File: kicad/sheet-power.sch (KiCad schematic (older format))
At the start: 18 parts, among them U13 AMS1117-3.3

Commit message: layout and bom complete - waiting on parts from jlcpcb
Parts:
- added D11: b5819w, Diode_SMD:D_SOD-123, symbol Device:D_Schottky_Small
- C31: value 10uf -> 10u; footprint (none) -> Capacitor_SMD:C_0603_1608Metric
- C32, C33, C34, C35, C36, C37, C38, C39, C40: value 100nf -> 100n; footprint (none) -> Capacitor_SMD:C_0402_1005Metric
- C41, C42: value 10uF -> 10u; footprint (none) -> Capacitor_SMD:C_0805_2012Metric
- C43: value 100nF -> 100n; footprint (none) -> Capacitor_SMD:C_0402_1005Metric
- C44: value 10uF -> 10n; footprint (none) -> Capacitor_SMD:C_0402_1005Metric
- D7: footprint (none) -> Diode_SMD:D_SOD-123
- FB1, FB2: footprint (none) -> Inductor_SMD:L_0805_2012Metric
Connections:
- net at D7.1 (K), FB1.2: now also D11.1 (K)
- new net ALT_POWER: D11.2 (A)
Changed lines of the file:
@@
 AR Path="/6020FDCC/60239D67" Ref="FB1"  Part="1"
 F 0 "FB1" V 1863 2950 50  0000 C CNN
-F 1 "100 @ 100Mhz" V 1954 2950 50  0000 C CNN
-F 2 "" V 2030 2950 50  0001 C CNN
+F 1 "100 @ 100Mhz" V 1950 3000 50  0000 C CNN
+F 2 "Inductor_SMD:L_0805_2012Metric" V 2030 2950 50  0001 C CNN
 F 3 "~" H 2100 2950 50  0001 C CNN
 	1    2100 2950
@@
 F 0 "D7" H 1650 2743 50  0000 C CNN
 F 1 "b5819w" H 1650 2834 50  0000 C CNN
-F 2 "" V 1650 2950 50  0001 C CNN
+F 2 "Diode_SMD:D_SOD-123" V 1650 2950 50  0001 C CNN
 F 3 "~" V 1650 2950 50  0001 C CNN
 	1    1650 2950
 	-1   0    0    1
 $EndComp
-Wire Wire Line
-	1750 2950 2000 2950
 $Comp
 L Device:C_Small C?
@@
 AR Path="/6020FDCC/60239D74" Ref="C41"  Part="1"
 F 0 "C41" H 2308 3104 50  0000 R CNN
-F 1 "10uF" H 2308 3195 50  0000 R CNN
-F 2 "" H 2400 3150 50  0001 C CNN
+F 1 "10u" H 2308 3195 50  0000 R CNN
+F 2 "Capacitor_SMD:C_0805_2012Metric" H 2400 3150 50  0001 C CNN
 F 3 "~" H 2400 3150 50  0001 C CNN
 	1    2400 3150
@@
 AR Path="/6020FDCC/60239D7A" Ref="C42"  Part="1"
 F 0 "C42" H 3308 3104 50  0000 R CNN
-F 1 "10uF" H 3308 3195 50  0000 R CNN
-F 2 "" H 3400 3150 50  0001 C CNN
+F 1 "10u" H 3308 3195 50  0000 R CNN
+F 2 "Capacitor_SMD:C_0805_2012Metric" H 3400 3150 50  0001 C CNN
 F 3 "~" H 3400 3150 50  0001 C CNN
 	1    3400 3150
@@
 AR Path="/6020FDCC/60239D9D" Ref="C34"  Part="1"
 F 0 "C34" H 5558 3054 50  0000 R CNN
-F 1 "100nf" H 5558 3145 50  0000 R CNN
-F 2 "" H 5650 3100 50  0001 C CNN
+F 1 "100n" H 5558 3145 50  0000 R CNN
+F 2 "Capacitor_SMD:C_0402_1005Metric" H 5650 3100 50  0001 C CNN
 F 3 "~" H 5650 3100 50  0001 C CNN
 	1    5650 3100
@@
 AR Path="/6020FDCC/60239DA3" Ref="C35"  Part="1"
 F 0 "C35" H 5908 3054 50  0000 R CNN
-F 1 "100nf" H 5908 3145 50  0000 R CNN
-F 2 "" H 6000 3100 50  0001 C CNN
+F 1 "100n" H 5908 3145 50  0000 R CNN
+F 2 "Capacitor_SMD:C_0402_1005Metric" H 6000 3100 50  0001 C CNN
 F 3 "~" H 6000 3100 50  0001 C CNN
 	1    6000 3100
@@
 AR Path="/6020FDCC/60239DA9" Ref="C36"  Part="1"
 F 0 "C36" H 6258 3054 50  0000 R CNN
-F 1 "100nf" H 6258 3145 50  0000 R CNN
-F 2 "" H 6350 3100 50  0001 C CNN
+F 1 "100n" H 6258 3145 50  0000 R CNN
+F 2 "Capacitor_SMD:C_0402_1005Metric" H 6350 3100 50  0001 C CNN
 F 3 "~" H 6350 3100 50  0001 C CNN
 	1    6350 3100
@@
 AR Path="/6020FDCC/60239DAF" Ref="C37"  Part="1"
 F 0 "C37" H 6608 3054 50  0000 R CNN
-F 1 "100nf" H 6608 3145 50  0000 R CNN
-F 2 "" H 6700 3100 50  0001 C CNN
+F 1 "100n" H 6608 3145 50  0000 R CNN
+F 2 "Capacitor_SMD:C_0402_1005Metric" H 6700 3100 50  0001 C CNN
 F 3 "~" H 6700 3100 50  0001 C CNN
 	1    6700 3100
@@
 AR Path="/6020FDCC/60239DB5" Ref="C38"  Part="1"
 F 0 "C38" H 6908 3054 50  0000 R CNN
-F 1 "100nf" H 6908 3145 50  0000 R CNN
-F 2 "" H 7000 3100 50  0001 C CNN
+F 1 "100n" H 6908 3145 50  0000 R CNN
+F 2 "Capacitor_SMD:C_0402_1005Metric" H 7000 3100 50  0001 C CNN
 F 3 "~" H 7000 3100 50  0001 C CNN
 	1    7000 3100
@@
 AR Path="/6020FDCC/60239DBB" Ref="C39"  Part="1"
 F 0 "C39" H 7208 3054 50  0000 R CNN
-F 1 "100nf" H 7208 3145 50  0000 R CNN
-F 2 "" H 7300 3100 50  0001 C CNN
+F 1 "100n" H 7208 3145 50  0000 R CNN
+F 2 "Capacitor_SMD:C_0402_1005Metric" H 7300 3100 50  0001 C CNN
 F 3 "~" H 7300 3100 50  0001 C CNN
 	1    7300 3100
@@
 AR Path="/6020FDCC/60239DC1" Ref="C33"  Part="1"
 F 0 "C33" H 5258 3054 50  0000 R CNN
-F 1 "100nf" H 5258 3145 50  0000 R CNN
-F 2 "" H 5350 3100 50  0001 C CNN
+F 1 "100n" H 5258 3145 50  0000 R CNN
+F 2 "Capacitor_SMD:C_0402_1005Metric" H 5350 3100 50  0001 C CNN
 F 3 "~" H 5350 3100 50  0001 C CNN
 	1    5350 3100
@@
 AR Path="/6020FDCC/60239DC7" Ref="C32"  Part="1"
 F 0 "C32" H 4958 3054 50  0000 R CNN
-F 1 "100nf" H 4958 3145 50  0000 R CNN
-F 2 "" H 5050 3100 50  0001 C CNN
+F 1 "100n" H 4958 3145 50  0000 R CNN
+F 2 "Capacitor_SMD:C_0402_1005Metric" H 5050 3100 50  0001 C CNN
 F 3 "~" H 5050 3100 50  0001 C CNN
 	1    5050 3100
@@
 AR Path="/6020FDCC/60239DCD" Ref="C31"  Part="1"
 F 0 "C31" H 4658 3054 50  0000 R CNN
-F 1 "10uf" H 4658 3145 50  0000 R CNN
-F 2 "" H 4750 3100 50  0001 C CNN
+F 1 "10u" H 4658 3145 50  0000 R CNN
+F 2 "Capacitor_SMD:C_0603_1608Metric" H 4750 3100 50  0001 C CNN
 F 3 "~" H 4750 3100 50  0001 C CNN
 	1    4750 3100
@@
 AR Path="/6020FDCC/60239E13" Ref="C40"  Part="1"
 F 0 "C40" H 7558 3054 50  0000 R CNN
-F 1 "100nf" H 7558 3145 50  0000 R CNN
-F 2 "" H 7650 3100 50  0001 C CNN
+F 1 "100n" H 7558 3145 50  0000 R CNN
+F 2 "Capacitor_SMD:C_0402_1005Metric" H 7650 3100 50  0001 C CNN
 F 3 "~" H 7650 3100 50  0001 C CNN
 	1    7650 3100
@@
 U 1 1 6025CC61
 P 9150 2950
-F 0 "FB2" V 8913 2950 50  0000 C CNN
-F 1 "100 @ 100Mhz" V 9004 2950 50  0000 C CNN
-F 2 "" V 9080 2950 50  0001 C CNN
+F 0 "FB2" V 9050 3050 50  0000 C CNN
+F 1 "100 @ 100Mhz" V 9250 2900 50  0000 C CNN
+F 2 "Inductor_SMD:L_0805_2012Metric" V 9080 2950 50  0001 C CNN
 F 3 "~" H 9150 2950 50  0001 C CNN
 	1    9150 2950
@@
 P 10000 3150
 F 0 "C44" H 9908 3104 50  0000 R CNN
-F 1 "10uF" H 9908 3195 50  0000 R CNN
-F 2 "" H 10000 3150 50  0001 C CNN
+F 1 "10n" H 9908 3195 50  0000 R CNN
+F 2 "Capacitor_SMD:C_0402_1005Metric" H 10000 3150 50  0001 C CNN
 F 3 "~" H 10000 3150 50  0001 C CNN
 	1    10000 3150
@@
 P 9600 3150
 F 0 "C43" H 9508 3104 50  0000 R CNN
-F 1 "100nF" H 9508 3195 50  0000 R CNN
-F 2 "" H 9600 3150 50  0001 C CNN
+F 1 "100n" H 9508 3195 50  0000 R CNN
+F 2 "Capacitor_SMD:C_0402_1005Metric" H 9600 3150 50  0001 C CNN
 F 3 "~" H 9600 3150 50  0001 C CNN
 	1    9600 3150
@@
 Text HLabel 10600 2950 2    50   Input ~ 0
 VREG_ANALOG
-Wire Wire Line
-	1100 2950 1350 2950
-Wire Wire Line
-	1350 2950 1550 2950
 Connection ~ 1350 2950
-Wire Wire Line
-	1350 2700 1350 2950
 $Comp
 L power:VCC #PWR?
@@
 Text Notes 1250 1250 0    50   ~ 0
 AMS1117-3.3  Sikor - should support 7s (30V)
+Wire Wire Line
+	1100 2950 1350 2950
+Wire Wire Line
+	1350 2700 1350 2950
+Wire Wire Line
+	1350 2950 1550 2950
+Wire Wire Line
+	1750 2950 1850 2950
+Wire Wire Line
+	1850 2700 1850 2950
+Connection ~ 1850 2950
+Wire Wire Line
+	1850 2950 2000 2950
+Text GLabel 2100 2350 2    50   Input ~ 0
+ALT_POWER
+$Comp
+L Device:D_Schottky_Small D?
+U 1 1 5FCF99E6
+P 1850 2600
+AR Path="/5FCF99E6" Ref="D?"  Part="1"
+AR Path="/6020FDCC/5FCF99E6" Ref="D11"  Part="1"
+F 0 "D11" H 1850 2393 50  0000 C CNN
+F 1 "b5819w" H 1850 2484 50  0000 C CNN
+F 2 "Diode_SMD:D_SOD-123" V 1850 2600 50  0001 C CNN
+F 3 "~" V 1850 2600 50  0001 C CNN
+	1    1850 2600
+	0    -1   -1   0
+$EndComp
+Wire Wire Line
+	1850 2350 1850 2500
+Wire Wire Line
+	2100 2350 1850 2350
 $EndSCHEMATC

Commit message: Adding 0.9 version
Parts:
- removed C41, C42: 10u, Capacitor_SMD:C_0805_2012Metric, symbol Device:C_Small
- removed D11: b5819w, Diode_SMD:D_SOD-123, symbol Device:D_Schottky_Small
- removed U13: AMS1117-3.3, Package_TO_SOT_SMD:SOT-223-3_TabPin2, symbol Regulator_Linear:AMS1117-3.3
- added C11: 100n, Capacitor_SMD:C_0402_1005Metric, symbol Device:C_Small
- added C12: 10u, Capacitor_SMD:C_0402_1005Metric, symbol Device:C_Small
- added C13: 4.7u+, Capacitor_SMD:C_0805_2012Metric, symbol Device:C_Small
- added C59: 33p, Capacitor_SMD:C_0402_1005Metric, symbol Device:C_Small
- added C60: 1000u+, Capacitor_THT:CP_Radial_D8.0mm_P5.00mm, symbol Device:CP_Small
- added D5: b5819w, Diode_SMD:D_SOD-123, symbol Device:D_Schottky_Small
- added L1: 2.2uh, Inductor_SMD:L_1210_3225Metric, symbol Device:L_Small
- added R45: 400K, Resistor_SMD:R_0402_1005Metric, symbol Device:R_Small
- added R49: 120k, Resistor_SMD:R_0402_1005Metric, symbol Device:R_Small
- added R50: 39k, Resistor_SMD:R_0402_1005Metric, symbol Device:R_Small
- added U1: mp2451dt, Package_TO_SOT_SMD:SOT-23-6, symbol driva:mp2451dt
- renumbered C31 to C1, C40 to C10, C43 to C14, C44 to C15, C32 to C2, C33 to C3, C34 to C4, C35 to C5, C36 to C6, C37 to C7, C38 to C8, C39 to C9, D7 to D1
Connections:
- net +3V3: now also C12.2, C59.2, L1.2, R49.1
- net GND: now also C12.1, C13.1, C60.2, D5.2 (A), R50.2, U1.2 (GND)
- net VCC: now also C60.1
- net at FB1.1: now also C13.2, R45.2, U1.5 (VIN)
- new net: R45.1, U1.4 (EN)
- new net: C11.2, U1.1 (BOOST)
- new net: C59.1, R49.2, R50.1, U1.3 (FB)
- new net: C11.1, D5.1 (K), L1.1, U1.6 (SW)
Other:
- note added: "Supply -> 3.3 Step Down"
- note removed: "+3.3V Voltage Regulation"
- note removed: "AMS1117-3.3 Sikor - should support 7s (30V)"
- moved on the sheet: C1, C10, C14, C15, C2, C3, C4, C5, C6, C7, C8, C9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

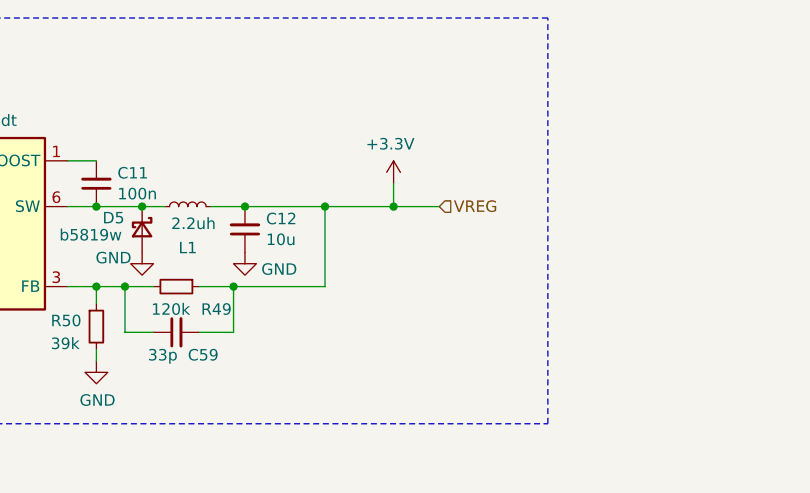
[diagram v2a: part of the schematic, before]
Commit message: adding solder bridge and more vias under driver
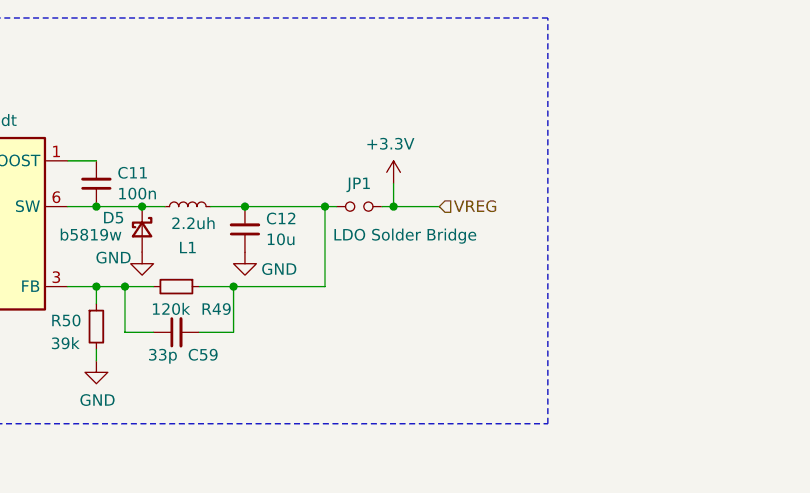
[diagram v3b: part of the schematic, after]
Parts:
- added JP1: LDO Solder Bridge, symbol Device:Jumper_NO_Small
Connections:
- net +3V3: now also JP1.2; no longer C12.2, C59.2, L1.2, R49.1
- new net: C12.2, C59.2, JP1.1, L1.2, R49.1
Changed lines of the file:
@@
 	-1   0    0    -1
 $EndComp
-Connection ~ 8300 2200
-Wire Wire Line
-	8300 2200 8600 2200
 Wire Wire Line
 	8600 2200 8600 2100
@@
 Wire Wire Line
 	8800 2200 8600 2200
-Connection ~ 8600 2200
 Wire Wire Line
 	4975 2050 5150 2050
@@
 Wire Wire Line
 	4775 2825 5600 2825
+$Comp
+L Device:Jumper_NO_Small JP1
+U 1 1 6021E190
+P 8450 2200
+F 0 "JP1" H 8450 2300 50  0000 C CNN
+F 1 "LDO Solder Bridge" H 8650 2075 50  0000 C CNN
+F 2 "" H 8450 2200 50  0001 C CNN
+F 3 "~" H 8450 2200 50  0001 C CNN
+	1    8450 2200
+	1    0    0    -1
+$EndComp
+Wire Wire Line
+	8550 2200 8600 2200
+Connection ~ 8600 2200
+Wire Wire Line
+	8350 2200 8300 2200
+Connection ~ 8300 2200
 $EndSCHEMATC

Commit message: updating bom and pos files
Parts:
- JP1: footprint (none) -> Jumper:SolderJumper-2_P1.3mm_Bridged_Pad1.0x1.5mm
- R45: value 400K -> 300K
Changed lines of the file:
@@
 P 6175 2200
 F 0 "R45" H 6325 2175 50  0000 C CNN
-F 1 "400K" H 6325 2250 50  0000 C CNN
+F 1 "300K" H 6325 2250 50  0000 C CNN
 F 2 "Resistor_SMD:R_0402_1005Metric" H 6175 2200 50  0001 C CNN
 F 3 "~" H 6175 2200 50  0001 C CNN
@@
 F 0 "JP1" H 8450 2300 50  0000 C CNN
 F 1 "LDO Solder Bridge" H 8650 2075 50  0000 C CNN
-F 2 "" H 8450 2200 50  0001 C CNN
+F 2 "Jumper:SolderJumper-2_P1.3mm_Bridged_Pad1.0x1.5mm" H 8450 2200 50  0001 C CNN
 F 3 "~" H 8450 2200 50  0001 C CNN
 	1    8450 2200
